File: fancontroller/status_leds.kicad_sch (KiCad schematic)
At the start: 12 parts

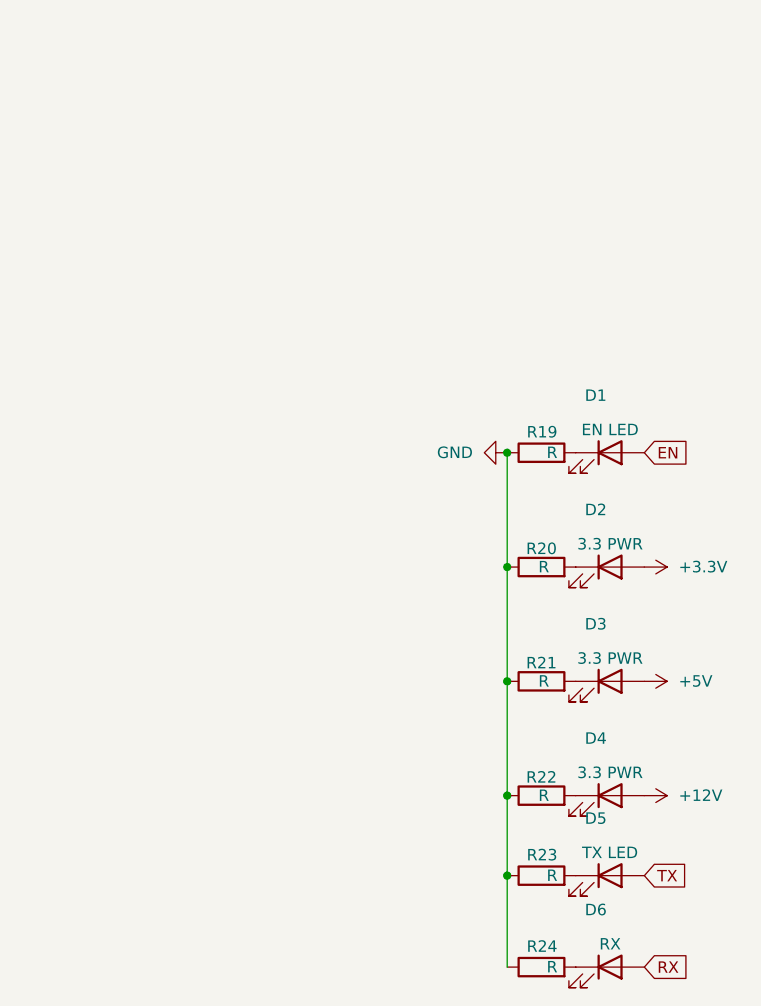
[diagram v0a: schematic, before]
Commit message: Restructure Fan drivers into separate modules and rework USB-C
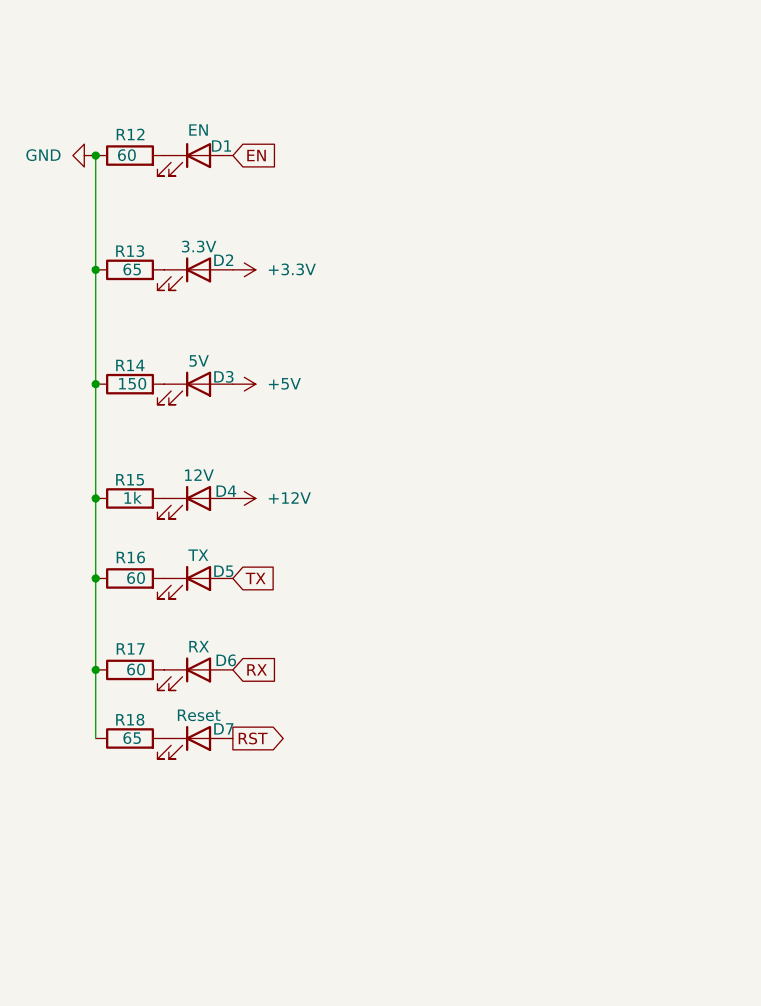
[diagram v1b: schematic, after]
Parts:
- added D7: Reset, symbol Device:LED
- added R18: 65, symbol Device:R
- D1: value EN LED -> EN; LCSC Part # (none) -> C84257
- D2: value 3.3 PWR -> 3.3V; LCSC Part # (none) -> C84262
- D3: value 3.3 PWR -> 5V; LCSC Part # (none) -> C84262
- D4: value 3.3 PWR -> 12V; LCSC Part # (none) -> C84256
- D5: value TX LED -> TX; LCSC Part # (none) -> C84257
- D6: LCSC Part # (none) -> C84257
- R12: renamed from R19; value R -> 60
- R13: renamed from R20; value R -> 65
- R14: renamed from R21; value R -> 150
- R15: renamed from R22; value R -> 1k; footprint (none) -> Resistor_SMD:R_0805_2012Metric; LCSC Part # (none) -> C17513
- R16: renamed from R23; value R -> 60
- R17: renamed from R24; value R -> 60
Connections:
- net GND: now also R18.1
- new net: D7.1 (K), R18.2
- new net RST: D7.2 (A)
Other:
- company: (none) -> DJ-Bauer
- title: (none) -> Status LED batch
- moved on the sheet: D1, D2, D3, D4, D5, D6, R12, R13, R14, R15, R16, R17

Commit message: Improve footprints and do massive overhaul for part numbering for better future order
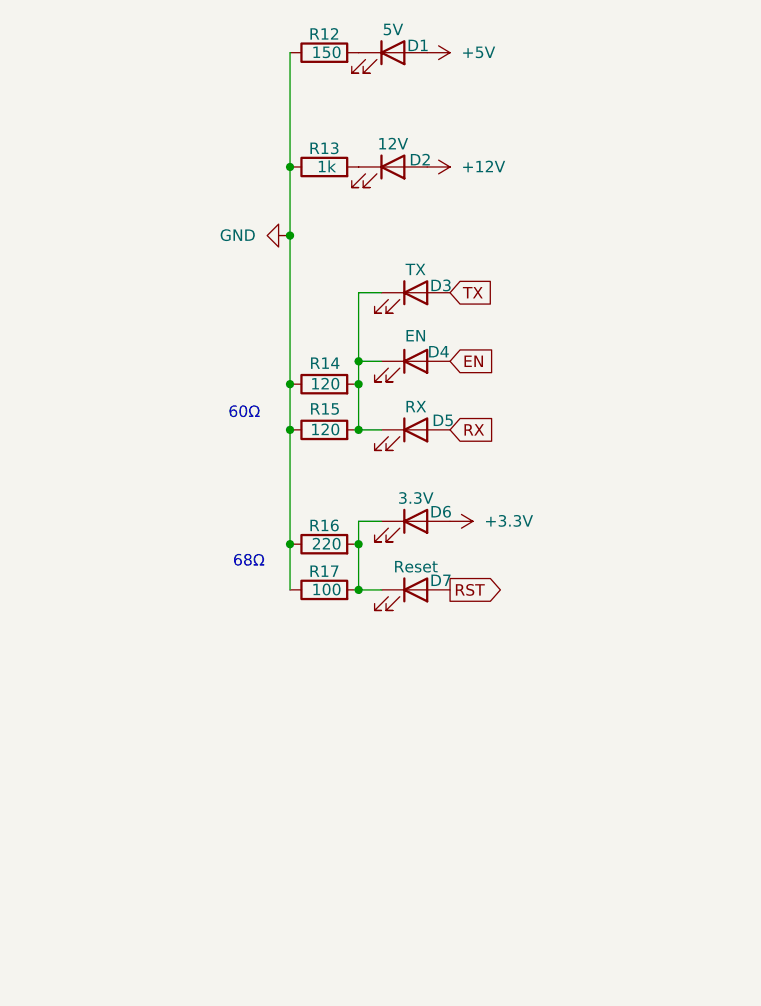
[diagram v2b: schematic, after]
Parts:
- removed R12: 60, Resistor_SMD:R_0805_2012Metric, symbol Device:R
- removed R13: 65, symbol Device:R
- added R14: 120, Resistor_SMD:R_0805_2012Metric, symbol Device:R
- D1: renamed from D3; footprint (none) -> LED_SMD:LED_0805_2012Metric
- D2: renamed from D4; footprint (none) -> LED_SMD:LED_0805_2012Metric
- D3: renamed from D5; footprint (none) -> LED_SMD:LED_0805_2012Metric
- D4: renamed from D1; footprint (none) -> LED_SMD:LED_0805_2012Metric
- D5: renamed from D6; footprint (none) -> LED_SMD:LED_0805_2012Metric
- D6: renamed from D2; footprint (none) -> LED_SMD:LED_0805_2012Metric
- D7: footprint (none) -> LED_SMD:LED_0805_2012Metric
- R12: renamed from R14; footprint (none) -> Resistor_SMD:R_0805_2012Metric; LCSC Part # (none) -> C17471
- R15: renamed from R17; value 60 -> 120; LCSC Part # C17513 -> C17437
- R16: value 60 -> 220; footprint Resistor_SMD:R_0805_2012Metric -> Resistor_SMD:R_0603_1608Metric; LCSC Part # C17513 -> C17557
- R17: renamed from R18; value 65 -> 100; footprint (none) -> Resistor_SMD:R_0603_1608Metric; LCSC Part # (none) -> C17408
- renumbered R15 to R13
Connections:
- net GND: now also R14.1
- net at D6.1 (K): now also D7.1 (K), R16.2, R17.2
- net at D3.1 (K): now also D4.1 (K), D5.1 (K), R15.2, R14.2; no longer R16.2
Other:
- note added: "60Ω"
- note added: "68Ω"
- moved on the sheet: D1, D2, D3, D4, D5, D6, D7, R12, R13, R15, R17
